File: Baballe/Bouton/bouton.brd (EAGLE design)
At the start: 30 x 32 mm, 12 parts, among them IC1 74AHC1G04DBV, Q1 IRF7319

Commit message: V2 de la Baballe
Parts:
- moved SUPPLY 41.6 mm to (70.9, 44.6)
- moved I/O 41.4 mm to (47.1, 44.4)
- moved IC1 39.6 mm to (58.0, 51.0), turned to 90 degrees
- moved BP3 38.4 mm to (47.0, 62.4)
- moved BP4 38.4 mm to (69.0, 62.4)
- moved BP1 38.4 mm to (47.0, 67.4)
- moved BP2 38.3 mm to (69.1, 67.3)
- moved R1 34.3 mm to (64.0, 42.3)
- moved Q1 34.0 mm to (58.0, 43.0)
- moved R2 33.6 mm to (52.0, 50.3), turned to 180 degrees
- moved R3 29.0 mm to (65.3, 45.7), turned to 270 degrees
- moved D1 28.6 mm to (53.0, 46.0), turned to 90 degrees
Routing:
- net N$2: track 3.49 -> 14.2 mm
- net V_ALIM: track 30.7 -> 41.3 mm, vias 1 -> 0
- net VS: track 53.9 -> 47.4 mm, vias 1 -> 0
- net I_BUTTON: track 4.13 -> 9.65 mm, vias 0 -> 1
- net N$1: track 17.8 -> 13.3 mm
- net V_BAT: track 62.0 -> 63.3 mm
- net O_POWER_CTRL: track 29.1 -> 30.3 mm, vias 1 -> 0
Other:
- board size 30 x 32 mm -> 38.1 x 38.1 mm

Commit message: Baballe en attente de vérification finale
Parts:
- moved SUPPLY 0.71 mm to (71.0, 43.9)
- moved I/O 0.40 mm to (47.1, 44.0)
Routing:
- net V_ALIM: track 41.3 -> 43.6 mm
- net O_POWER_CTRL: track 30.3 -> 29.6 mm
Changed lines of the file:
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@@
 <plain>
 <circle x="59" y="56" radius="19.026296875" width="0.1" layer="20"/>
-<circle x="59" y="56" radius="20.024984375" width="0.1" layer="47"/>
 <hole x="59" y="68" drill="15"/>
 </plain>
@@
 </autorouter>
 <elements>
-<element name="I/O" library="SparkFun-Connectors" package="1X06_NO_SILK" value="I/O" x="47.05533125" y="44.356" rot="R90">
-<attribute name="PROD_ID" value="CONN-08437" x="47.05533125" y="44.356" size="1.778" layer="27" rot="R90" display="off"/>
+<element name="I/O" library="SparkFun-Connectors" package="1X06_NO_SILK" value="I/O" x="47.05533125" y="43.956" rot="R90">
+<attribute name="PROD_ID" value="CONN-08437" x="47.05533125" y="43.956" size="1.778" layer="27" rot="R90" display="off"/>
 </element>
-<element name="SUPPLY" library="SparkFun-Connectors" package="1X05_NO_SILK" value="SUPPLY" x="70.9188625" y="44.626" rot="R90"/>
+<element name="SUPPLY" library="SparkFun-Connectors" package="1X05_NO_SILK" value="SUPPLY" x="71.0188625" y="43.926" rot="R90"/>
 <element name="BP1" library="SparkFun-Connectors" package="1X02_NO_SILK" value="BP1" x="47" y="67.365"/>
 <element name="BP2" library="SparkFun-Connectors" package="1X02_NO_SILK" value="BP2" x="69.08" y="67.3"/>
@@
 <wire x1="47.5" y1="52" x2="54" y2="52" width="0.3" layer="16"/>
 <wire x1="56.5" y1="52" x2="56.7" y2="51.95" width="0.3" layer="1"/>
-<wire x1="47.5" y1="52" x2="47.05533125" y2="51.976" width="0.3" layer="16"/>
+<wire x1="47.5" y1="52" x2="47.05533125" y2="51.576" width="0.3" layer="16"/>
 <via x="54" y="52" extent="1-16" drill="0.6096"/>
 </signal>
@@
 <wire x1="69.5" y1="49" x2="65.5" y2="45" width="0.5" layer="1"/>
 <wire x1="69.5" y1="51" x2="69.5" y2="49" width="0.5" layer="1"/>
-<wire x1="70.5" y1="52" x2="69.5" y2="51" width="0.5" layer="1"/>
+<wire x1="70.5" y1="51" x2="69.5" y2="51" width="0.5" layer="1"/>
 <wire x1="65.5" y1="45" x2="65.27" y2="44.83" width="0.5" layer="1"/>
-<wire x1="70.5" y1="52" x2="70.9188625" y2="52.246" width="0.5" layer="1"/>
+<wire x1="70.5" y1="51" x2="71.0188625" y2="51.546" width="0.5" layer="1"/>
 <wire x1="48" y1="62" x2="47" y2="62" width="0.5" layer="16"/>
 <wire x1="57.5" y1="52.5" x2="48" y2="62" width="0.5" layer="16"/>
@@
 <wire x1="69" y1="52.5" x2="57.5" y2="52.5" width="0.5" layer="16"/>
 <wire x1="47" y1="62" x2="47" y2="62.365" width="0.5" layer="16"/>
-<wire x1="70.5" y1="52.5" x2="70.9188625" y2="52.246" width="0.5" layer="16"/>
+<wire x1="70.5" y1="52.5" x2="71.0188625" y2="51.546" width="0.5" layer="16"/>
 <wire x1="69" y1="52.5" x2="69" y2="62.365" width="0.5" layer="16"/>
 </signal>
@@
 <wire x1="55.5" y1="43.5" x2="55.4568" y2="43.635" width="0.5" layer="1"/>
 <wire x1="55.5" y1="45" x2="55.4568" y2="44.905" width="0.5" layer="1"/>
-<wire x1="72.5" y1="49" x2="71" y2="47.5" width="0.5" layer="1"/>
-<wire x1="72.5" y1="55.5" x2="72.5" y2="49" width="0.5" layer="1"/>
-<wire x1="71.5" y1="56.5" x2="72.5" y2="55.5" width="0.5" layer="1"/>
-<wire x1="67.5" y1="56.5" x2="71.5" y2="56.5" width="0.5" layer="1"/>
+<wire x1="67.5" y1="56.5" x2="72.5" y2="56.5" width="0.5" layer="1"/>
 <wire x1="55.5" y1="44.5" x2="67.5" y2="56.5" width="0.5" layer="1"/>
-<wire x1="71" y1="47.5" x2="70.9188625" y2="47.166" width="0.5" layer="1"/>
+<wire x1="72" y1="46.5" x2="71.0188625" y2="46.466" width="0.5" layer="1"/>
+<wire x1="72.5" y1="56.5" x2="73" y2="56" width="0.5" layer="1"/>
+<wire x1="73" y1="56" x2="73" y2="47.5" width="0.5" layer="1"/>
+<wire x1="73" y1="47.5" x2="72" y2="46.5" width="0.5" layer="1"/>
 </signal>
 <signal name="O_POWER_CTRL">
@@
 <wire x1="54.5" y1="40" x2="56" y2="40" width="0.3" layer="1"/>
 <wire x1="48.5" y1="46" x2="54.5" y2="40" width="0.3" layer="1"/>
-<wire x1="48.5" y1="56" x2="48.5" y2="46" width="0.3" layer="1"/>
-<wire x1="47.5" y1="57" x2="48.5" y2="56" width="0.3" layer="1"/>
+<wire x1="48.5" y1="55" x2="48.5" y2="46" width="0.3" layer="1"/>
+<wire x1="47.5" y1="56" x2="48.5" y2="55" width="0.3" layer="1"/>
 <wire x1="60.5" y1="42.5" x2="60.5432" y2="42.365" width="0.3" layer="1"/>
-<wire x1="47.5" y1="57" x2="47.05533125" y2="57.056" width="0.3" layer="1"/>
+<wire x1="47.5" y1="56" x2="47.05533125" y2="56.656" width="0.3" layer="1"/>
 </signal>
 <signal name="N$1">

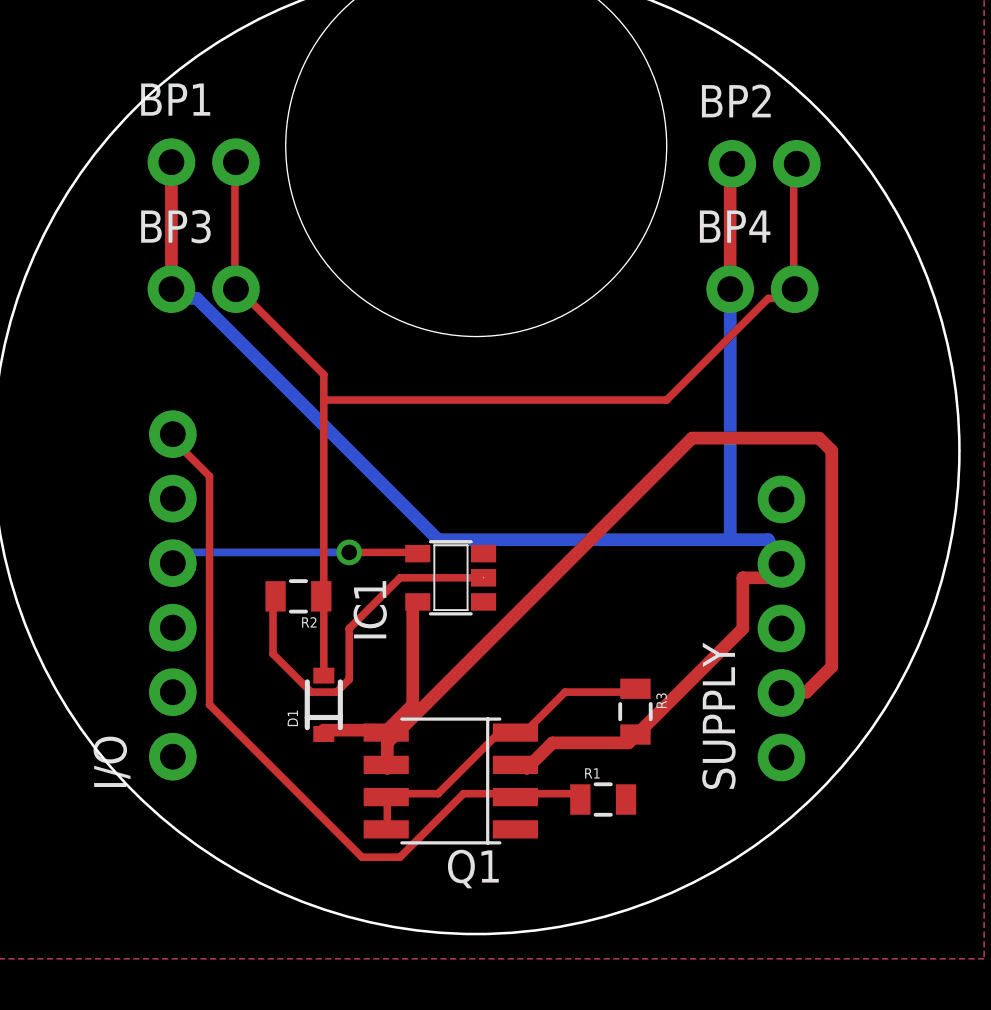
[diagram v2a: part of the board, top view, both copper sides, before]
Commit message: Correction des cartes alim et boutons suite à une erreur détectée lors de l'impression
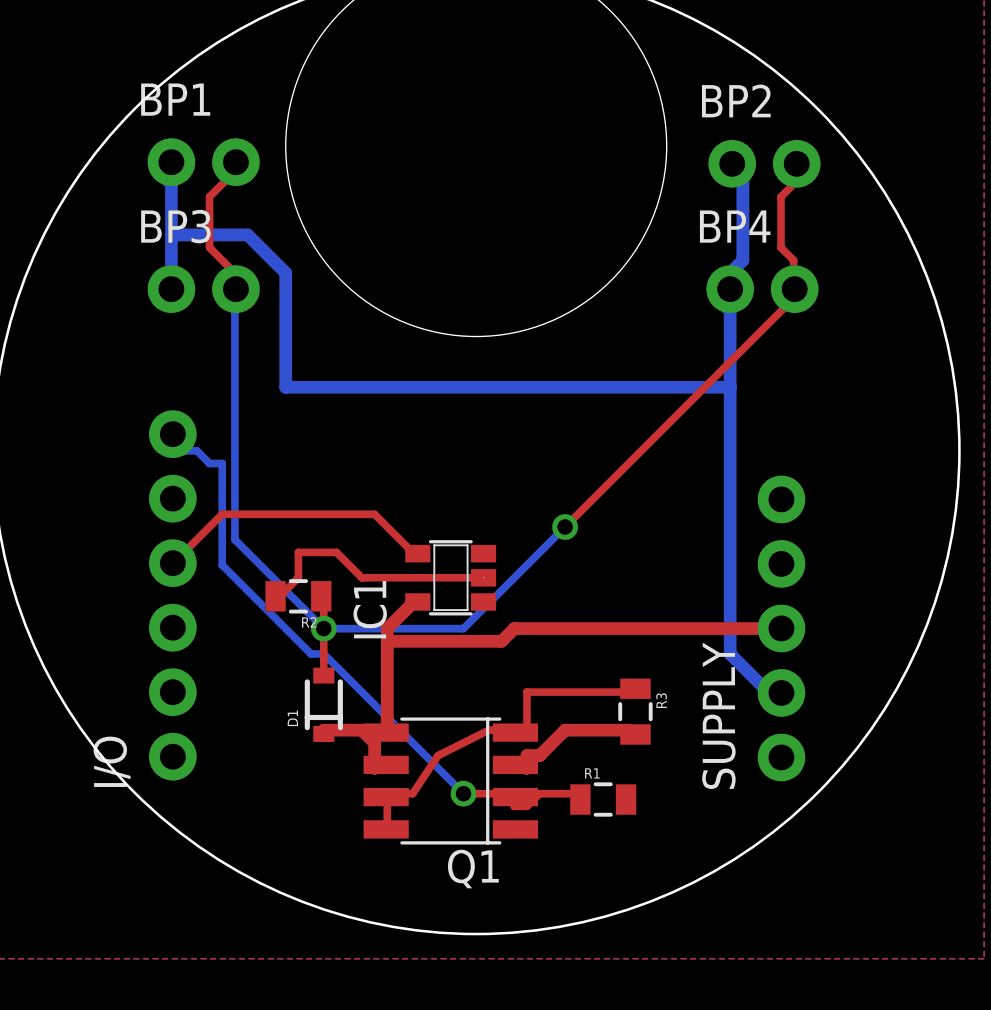
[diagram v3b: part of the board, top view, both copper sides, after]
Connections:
- new net V_IN: BP1.1, BP2.1, BP3.1, BP4.1, SUPPLY.2
- net V_ALIM: now also SUPPLY.3; no longer SUPPLY.2
- net V_BAT: no longer BP1.1, BP2.1, BP3.1, BP4.1, SUPPLY.4
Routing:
- net V_BAT: track 63.7 -> 5.71 mm
- net V_IN: track 0.00 -> 57.0 mm
- net V_ALIM: track 43.6 -> 26.3 mm
- net VS: track 47.4 -> 54.6 mm, vias 0 -> 2
- net O_POWER_CTRL: track 29.6 -> 25.4 mm, vias 0 -> 1
- net N$2: track 14.2 -> 10.4 mm
- net I_BUTTON: track 9.82 -> 11.1 mm, vias 1 -> 0
- net N$1: track 13.3 -> 14.2 mm
